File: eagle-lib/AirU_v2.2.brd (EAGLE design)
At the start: 71.1 x 79.4 mm, 86 parts, among them Q1 BSS138W-7-F, Q2 MMBT3904LT1G, Q3 MMBT3904LT1G, Q5 NCE3407A, U1 HDC1080DMBT, U2 CH340T-SSOP20, U3 CJT1117-3.3-SOT223, U4 MAX2659-DFN6, U5 L70-M39, U6 MOLEX-53261-0871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

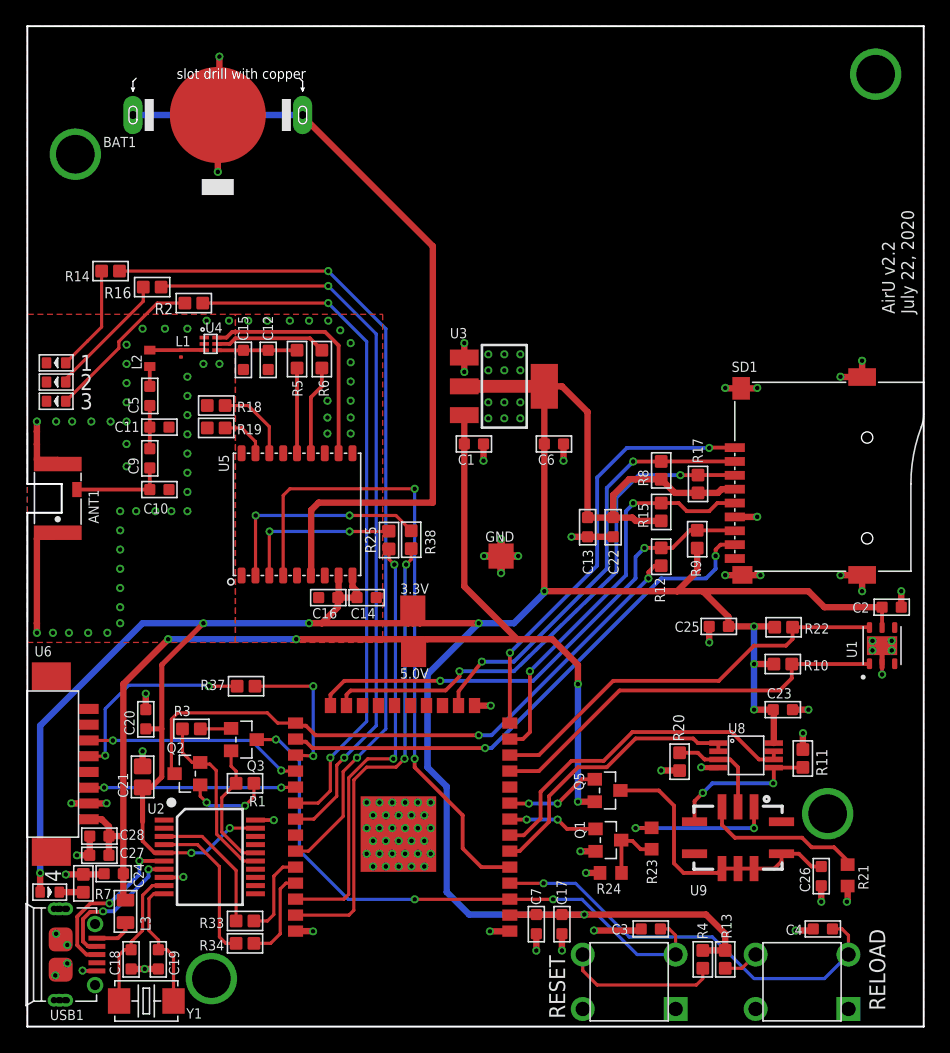
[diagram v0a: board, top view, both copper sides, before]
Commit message: board update
PM SET/RESET moved to RTC GPIO pins, MiCS pins swapped to avoid cross-over, sd moved to bottom, usb-uart moved to bottom, gps moved, temp sensor moved to avoid overheating, 5v-3.3v converter moved, 3.3V rail size increased for heat dissipation, tetrad logo added, buttons moved
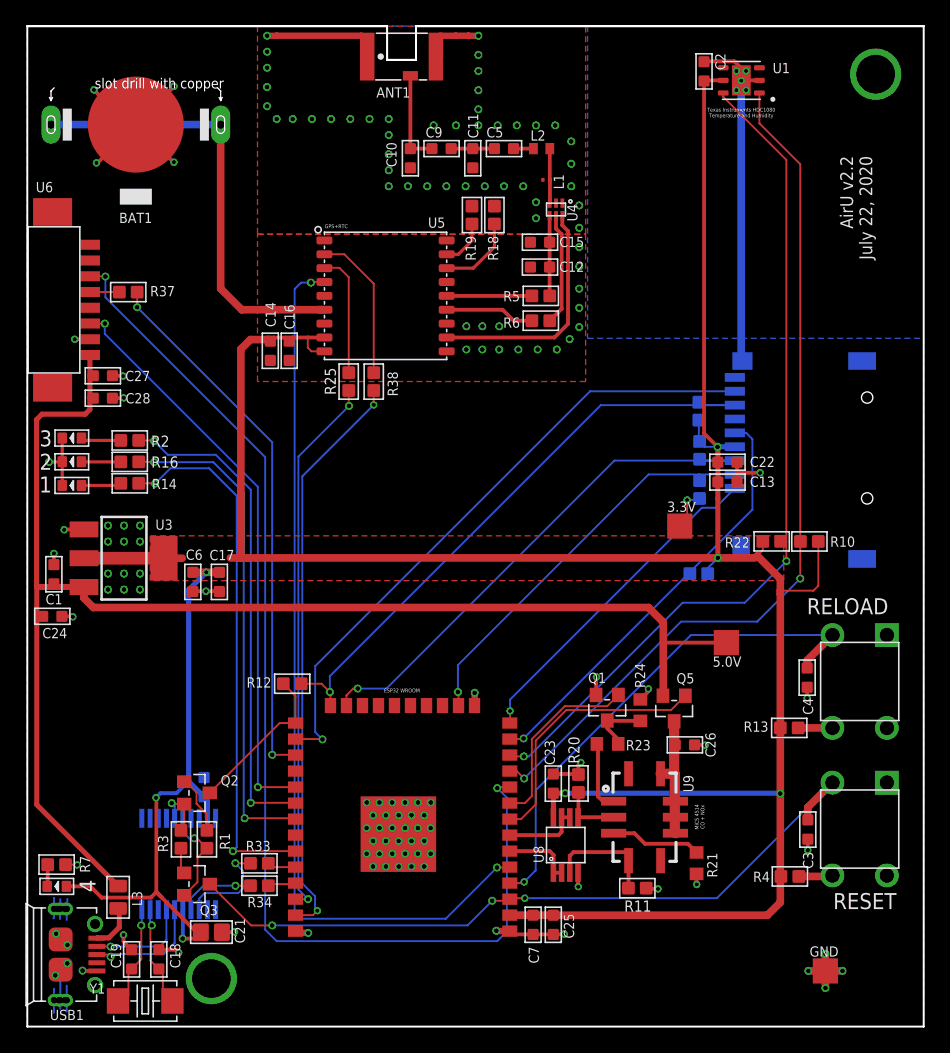
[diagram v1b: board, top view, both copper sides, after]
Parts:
- moved U1 46.2 mm to (56.7, 75.1), turned to 180 degrees
- moved C2 45.0 mm to (53.7, 75.8), turned to 0 degrees
- moved ANT1 44.4 mm to (29.7, 77.0), turned to 270 degrees
- moved GND 41.8 mm to (63.3, 4.42)
- moved C17 38.4 mm to (15.2, 35.3)
- moved C27 38.1 mm to (5.99, 51.6), turned to 270 degrees
- moved U6 36.8 mm to (4.17, 57.7)
- moved L2 35.3 mm to (40.8, 69.7), turned to 180 degrees
- moved C1 34.9 mm to (2.11, 35.9), turned to 0 degrees
- moved C28 34.7 mm to (5.99, 49.9), turned to 270 degrees
- moved C5 34.3 mm to (37.8, 69.7), turned to 270 degrees
- moved C9 33.8 mm to (32.9, 69.7), turned to 270 degrees
- moved U3 33.1 mm to (7.67, 37.2)
- moved C10 33.0 mm to (30.4, 68.9), turned to 180 degrees
- moved C11 32.8 mm to (35.3, 68.9), turned to 180 degrees
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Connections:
- net MICS_PREHEAT_NOX: now also U7.9; no longer U7.8
- net MICS_PWR: now also U7.8; no longer U7.9
- net PM_RESET: now also U7.10; no longer U7.28
- net VOX_RAWA: now also U8.5; no longer U8.3
- net VOX_RAWB: now also U7.7, U8.6, U8.7; no longer U7.6, U8.1, U8.2
- net VRED_RAWA: now also U8.3; no longer U8.5
- net VRED_RAWB: now also U7.6, U8.1, U8.2; no longer U7.7, U8.6, U8.7
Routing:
- net PM_RESET: track 17.4 -> 90.9 mm
- net GND: track 97.7 -> 135.9 mm, vias 162 -> 150
- net GPIO0: track 50.1 -> 12.6 mm, vias 2 -> 0
- net SDA: track 32.7 -> 69.7 mm, vias 0 -> 2
- net SCL: track 33.3 -> 68.1 mm, vias 0 -> 2
- net U2RXD: track 11.6 -> 43.0 mm
- net PM_SET: track 16.4 -> 46.0 mm
- net V_BCKP: track 63.6 -> 35.4 mm
- net STAT_LED1: track 68.0 -> 42.5 mm
- net 5.0V: track 95.5 -> 118.3 mm, vias 4 -> 0
- net VRED_RAWB: track 27.1 -> 5.67 mm
- net STAT_LED2: track 60.7 -> 39.3 mm
- net 1PPS: track 51.5 -> 71.1 mm
- net VOX_RAWB: track 22.2 -> 6.03 mm
- net STAT_LED3: track 54.3 -> 38.9 mm
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- added copper zone on layer 1, net 3.3V
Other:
- outline, holes or cut-outs redrawn
- board text added: "ESP32 WROOM"
- board text added: "GPS+RTC"
- board text added: "MiCS 4514 CO + NOx"
- board text added: "Texas Instruments HDC1080 Temperature and Humidity"
